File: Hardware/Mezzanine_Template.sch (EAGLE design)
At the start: 6 parts

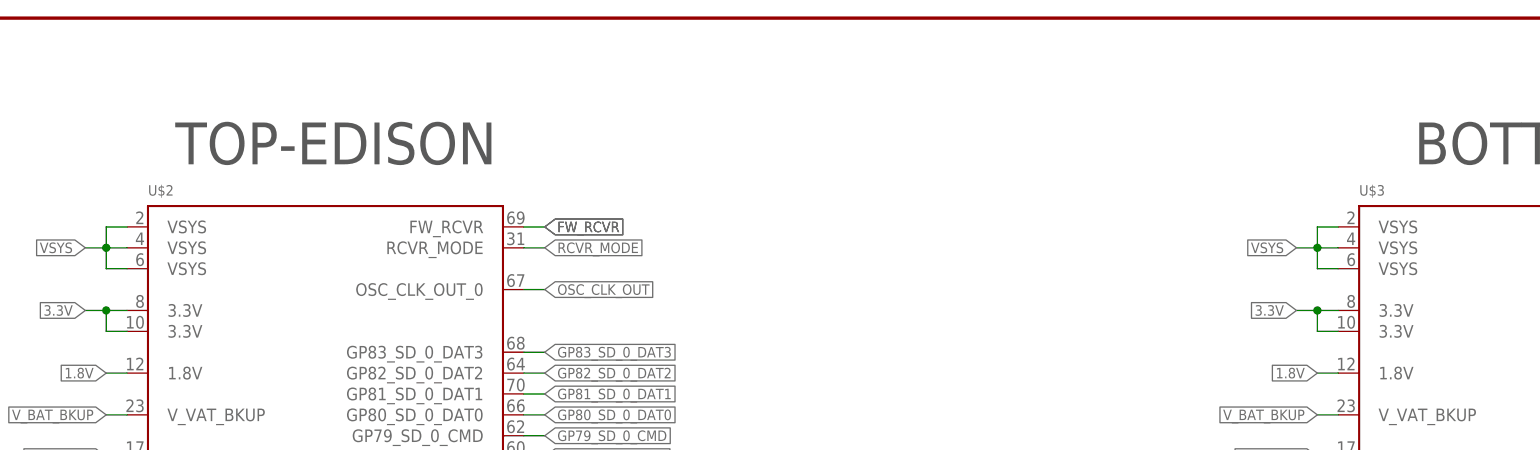
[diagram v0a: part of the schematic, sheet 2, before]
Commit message: Fixed $ in names, move name from silk to tNames
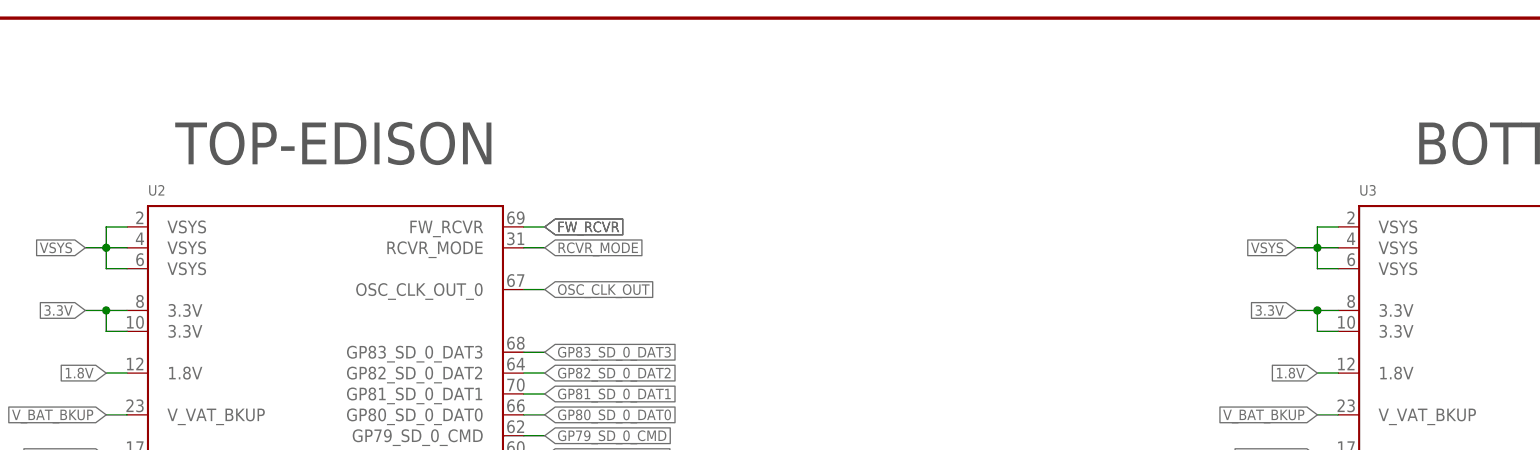
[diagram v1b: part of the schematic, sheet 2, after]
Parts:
- renumbered U$2 to U2, U$3 to U3

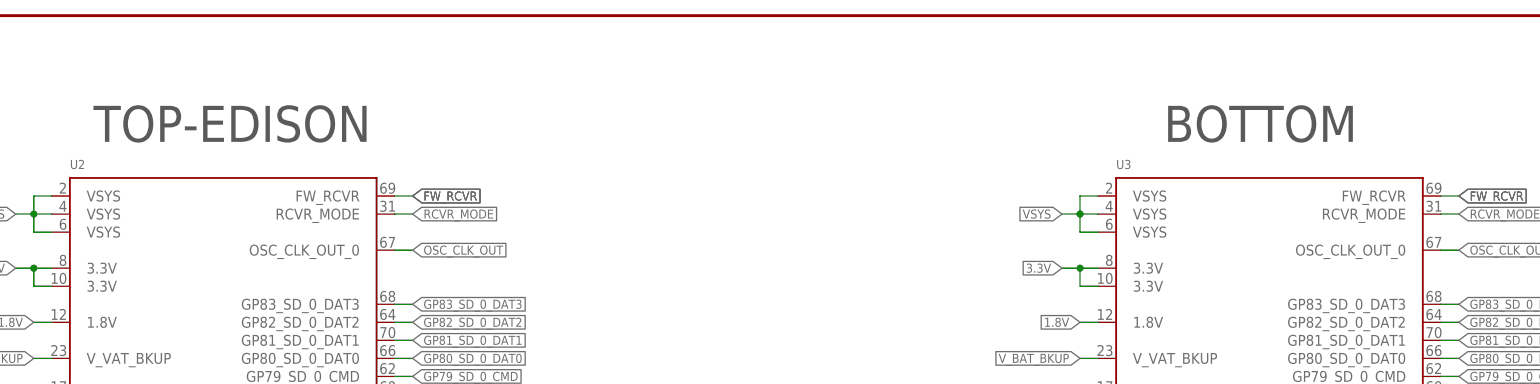
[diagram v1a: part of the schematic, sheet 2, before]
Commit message: added labels to clarify board orientation in schematic. updated library footprint for edision on demo board.
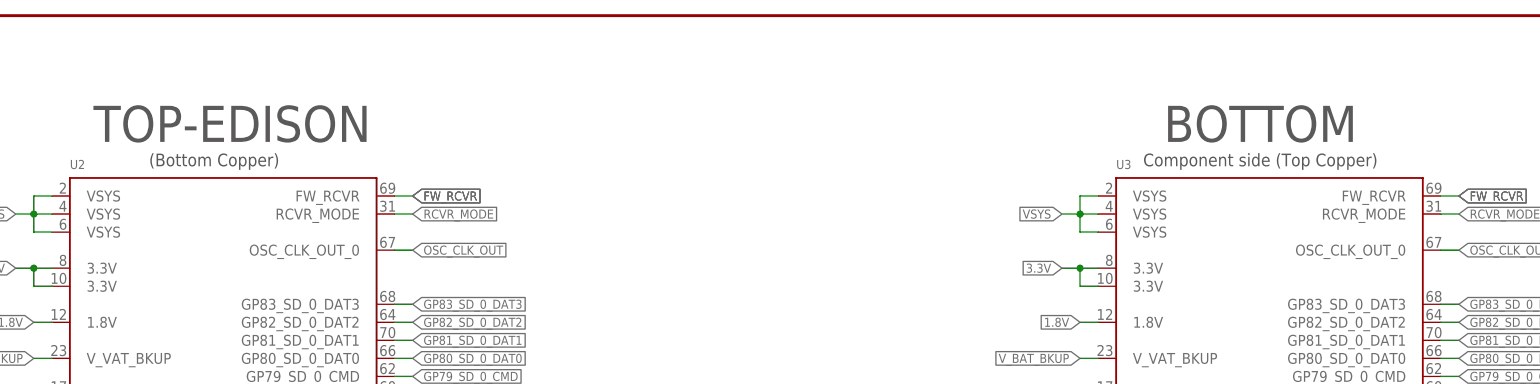
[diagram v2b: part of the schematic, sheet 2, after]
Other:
- note added: "(Bottom Copper)"
- note added: "Component side (Top Copper)"
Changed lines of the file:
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@@
 <text x="50.8" y="170.18" size="5.08" layer="92" align="center">TOP-EDISON</text>
 <text x="195.58" y="170.18" size="5.08" layer="92" align="center">BOTTOM</text>
+<text x="195.58" y="165.1" size="1.778" layer="92" align="center">Component side (Top Copper)</text>
+<text x="48.26" y="165.1" size="1.778" layer="92" align="center">(Bottom Copper)</text>
 </plain>
 <instances>

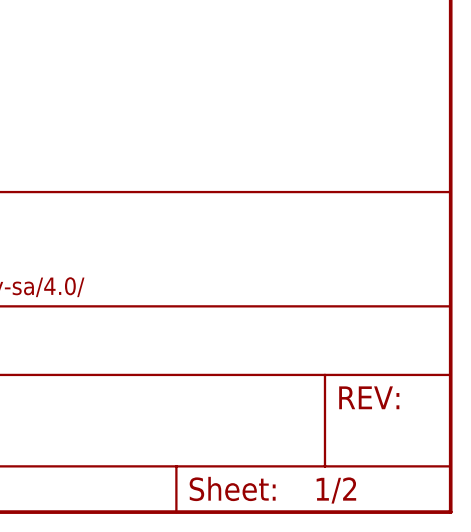
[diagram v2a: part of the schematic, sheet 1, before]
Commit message: added fiducials and second side logos to template
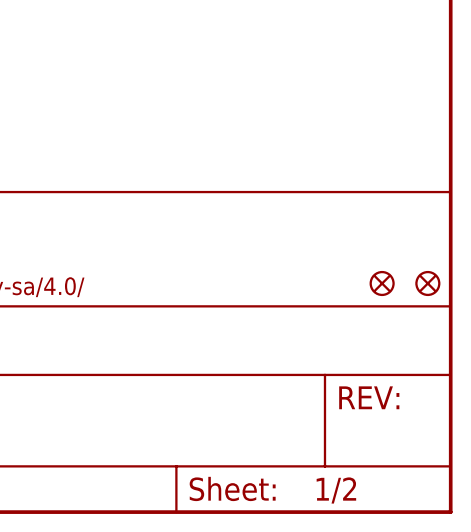
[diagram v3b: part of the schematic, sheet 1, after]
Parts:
- added FID1, FID2: FIDUCIAL1X2, SparkFun-Aesthetics:FIDUCIAL1X2
- renumbered LOGO2 to LOGO1, LOGO3 to LOGO4
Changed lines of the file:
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@@
 <parts>
 <part name="FRAME1" library="SparkFun-Aesthetics" deviceset="FRAME-LETTER" device=""/>
-<part name="LOGO2" library="SparkFun-Aesthetics" deviceset="OSHW-LOGO" device="S"/>
-<part name="LOGO3" library="SparkFun-Aesthetics" deviceset="SFE_LOGO_NAME_FLAME" device=".1_INCH"/>
+<part name="LOGO1" library="SparkFun-Aesthetics" deviceset="OSHW-LOGO" device="S"/>
+<part name="LOGO4" library="SparkFun-Aesthetics" deviceset="SFE_LOGO_NAME_FLAME" device=".1_INCH"/>
 <part name="U2" library="Edison" deviceset="EDISON_CONNECTOR_FULL" device="MOUNTING_HOLES"/>
 <part name="GND3" library="supply1" deviceset="GND" device=""/>
@@
 <part name="GND4" library="supply1" deviceset="GND" device=""/>
 <part name="FRAME2" library="SparkFun-Aesthetics" deviceset="FRAME-LETTER" device=""/>
+<part name="FID1" library="SparkFun-Aesthetics" deviceset="FIDUCIAL" device="1X2"/>
+<part name="FID2" library="SparkFun-Aesthetics" deviceset="FIDUCIAL" device="1X2"/>
 </parts>
 <sheets>
@@
 <instance part="FRAME1" gate="G$1" x="0" y="0"/>
 <instance part="FRAME1" gate="G$2" x="147.32" y="0"/>
-<instance part="LOGO2" gate="G$1" x="73.66" y="12.7"/>
-<instance part="LOGO3" gate="G$1" x="88.9" y="2.54"/>
+<instance part="LOGO1" gate="G$1" x="73.66" y="12.7"/>
+<instance part="LOGO4" gate="G$1" x="88.9" y="2.54"/>
+<instance part="FID1" gate="G$1" x="246.38" y="25.4"/>
+<instance part="FID2" gate="G$1" x="241.3" y="25.4"/>
 </instances>
 <busses>

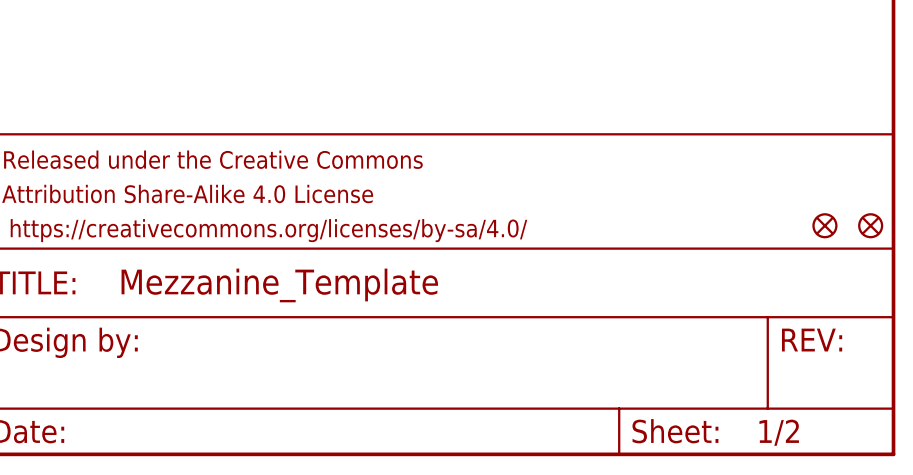
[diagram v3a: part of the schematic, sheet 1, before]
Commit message: - Added fiducials to both sides - flipped side name template is on - corrected 1.8v trace that was not connected. - removed my name from the designed by, Replaced with "Engineer" - Added template rev number to SCH.
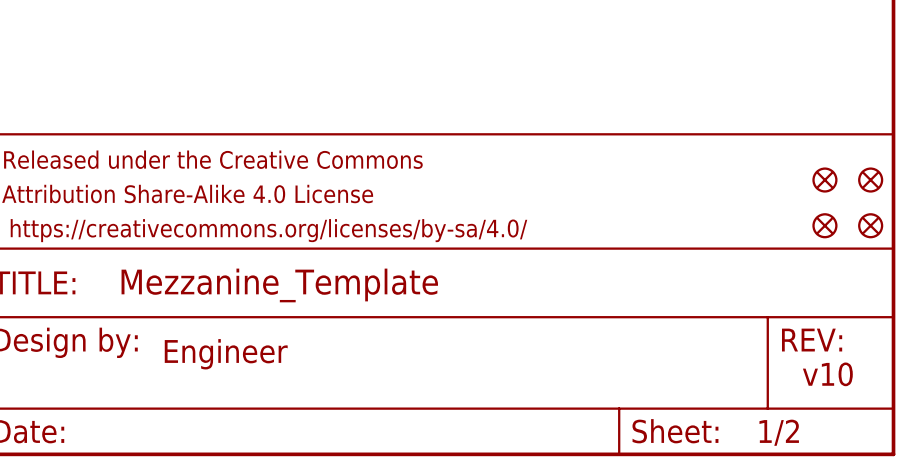
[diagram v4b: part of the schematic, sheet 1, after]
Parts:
- added FID3, FID4: FIDUCIAL1X2, SparkFun-Aesthetics:FIDUCIAL1X2
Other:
- note added: "Engineer"
- note added: "v10"
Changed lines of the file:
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@@
 <part name="FID1" library="SparkFun-Aesthetics" deviceset="FIDUCIAL" device="1X2"/>
 <part name="FID2" library="SparkFun-Aesthetics" deviceset="FIDUCIAL" device="1X2"/>
+<part name="FID3" library="SparkFun-Aesthetics" deviceset="FIDUCIAL" device="1X2"/>
+<part name="FID4" library="SparkFun-Aesthetics" deviceset="FIDUCIAL" device="1X2"/>
 </parts>
 <sheets>
 <sheet>
 <plain>
+<text x="238.76" y="7.62" size="2.54" layer="94">v10</text>
+<text x="167.64" y="10.16" size="2.54" layer="94">Engineer</text>
 </plain>
 <instances>
@@
 <instance part="FID1" gate="G$1" x="246.38" y="25.4"/>
 <instance part="FID2" gate="G$1" x="241.3" y="25.4"/>
+<instance part="FID3" gate="G$1" x="246.38" y="30.48"/>
+<instance part="FID4" gate="G$1" x="241.3" y="30.48"/>
 </instances>
 <busses>

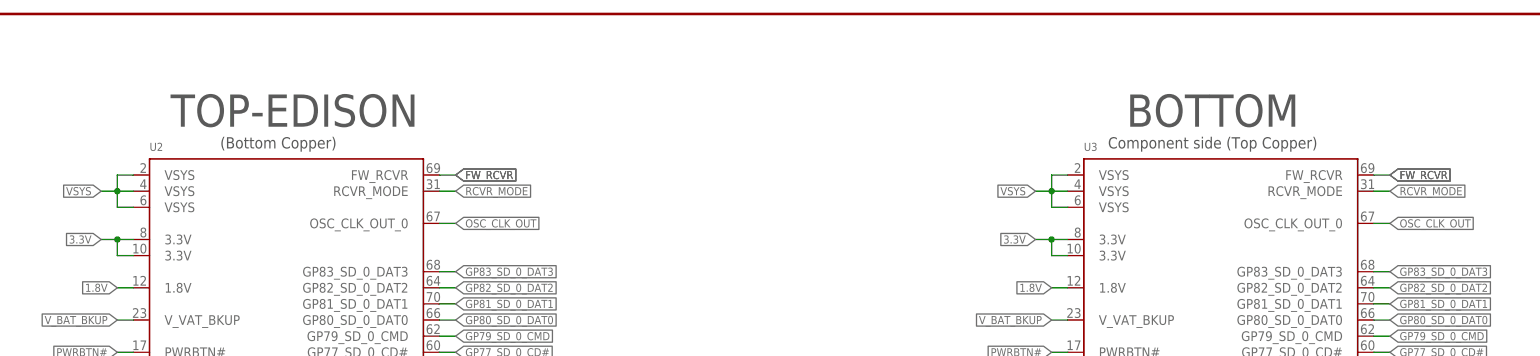
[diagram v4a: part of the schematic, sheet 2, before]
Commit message: corrected lables and removed extra packages that are no longer supported.
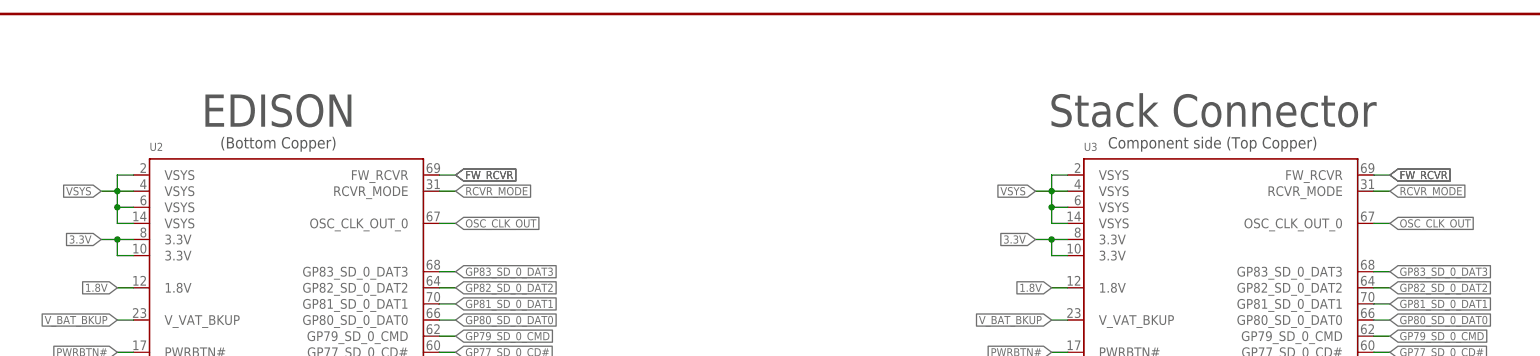
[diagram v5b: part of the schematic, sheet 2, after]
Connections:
- net VSYS: now also U2.VSYS@4, U3.VSYS@4
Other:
- note added: "EDISON"
- note added: "Stack Connector"
- note removed: "BOTTOM"
- note removed: "TOP-EDISON"
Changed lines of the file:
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@@
 <?xml version="1.0" encoding="utf-8"?>
 <!DOCTYPE eagle SYSTEM "eagle.dtd">
-<eagle version="6.5.0">
+<eagle version="6.6.0">
 <drawing>
 <settings>
@@
 <sheet>
 <plain>
-<text x="50.8" y="170.18" size="5.08" layer="92" align="center">TOP-EDISON</text>
-<text x="195.58" y="170.18" size="5.08" layer="92" align="center">BOTTOM</text>
+<text x="48.26" y="170.18" size="5.08" layer="92" align="center">EDISON</text>
+<text x="195.58" y="170.18" size="5.08" layer="92" align="center">Stack Connector</text>
 <text x="195.58" y="165.1" size="1.778" layer="92" align="center">Component side (Top Copper)</text>
 <text x="48.26" y="165.1" size="1.778" layer="92" align="center">(Bottom Copper)</text>
@@
 <wire x1="22.86" y1="157.48" x2="20.32" y2="157.48" width="0.1524" layer="91"/>
 <label x="20.32" y="157.48" size="1.27" layer="95" rot="R180" xref="yes"/>
+<wire x1="22.86" y1="154.94" x2="22.86" y2="152.4" width="0.1524" layer="91"/>
+<pinref part="U2" gate="G$1" pin="VSYS@4"/>
+<wire x1="22.86" y1="152.4" x2="25.4" y2="152.4" width="0.1524" layer="91"/>
+<junction x="22.86" y="154.94"/>
 </segment>
 <segment>
@@
 <wire x1="170.18" y1="157.48" x2="167.64" y2="157.48" width="0.1524" layer="91"/>
 <label x="167.64" y="157.48" size="1.27" layer="95" rot="R180" xref="yes"/>
+<pinref part="U3" gate="G$1" pin="VSYS@4"/>
+<wire x1="172.72" y1="152.4" x2="170.18" y2="152.4" width="0.1524" layer="91"/>
+<wire x1="170.18" y1="152.4" x2="170.18" y2="154.94" width="0.1524" layer="91"/>
+<junction x="170.18" y="154.94"/>
 </segment>
 </net>
